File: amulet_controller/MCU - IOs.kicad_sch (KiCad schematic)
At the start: 45 parts, among them U1 STM32G474RET3

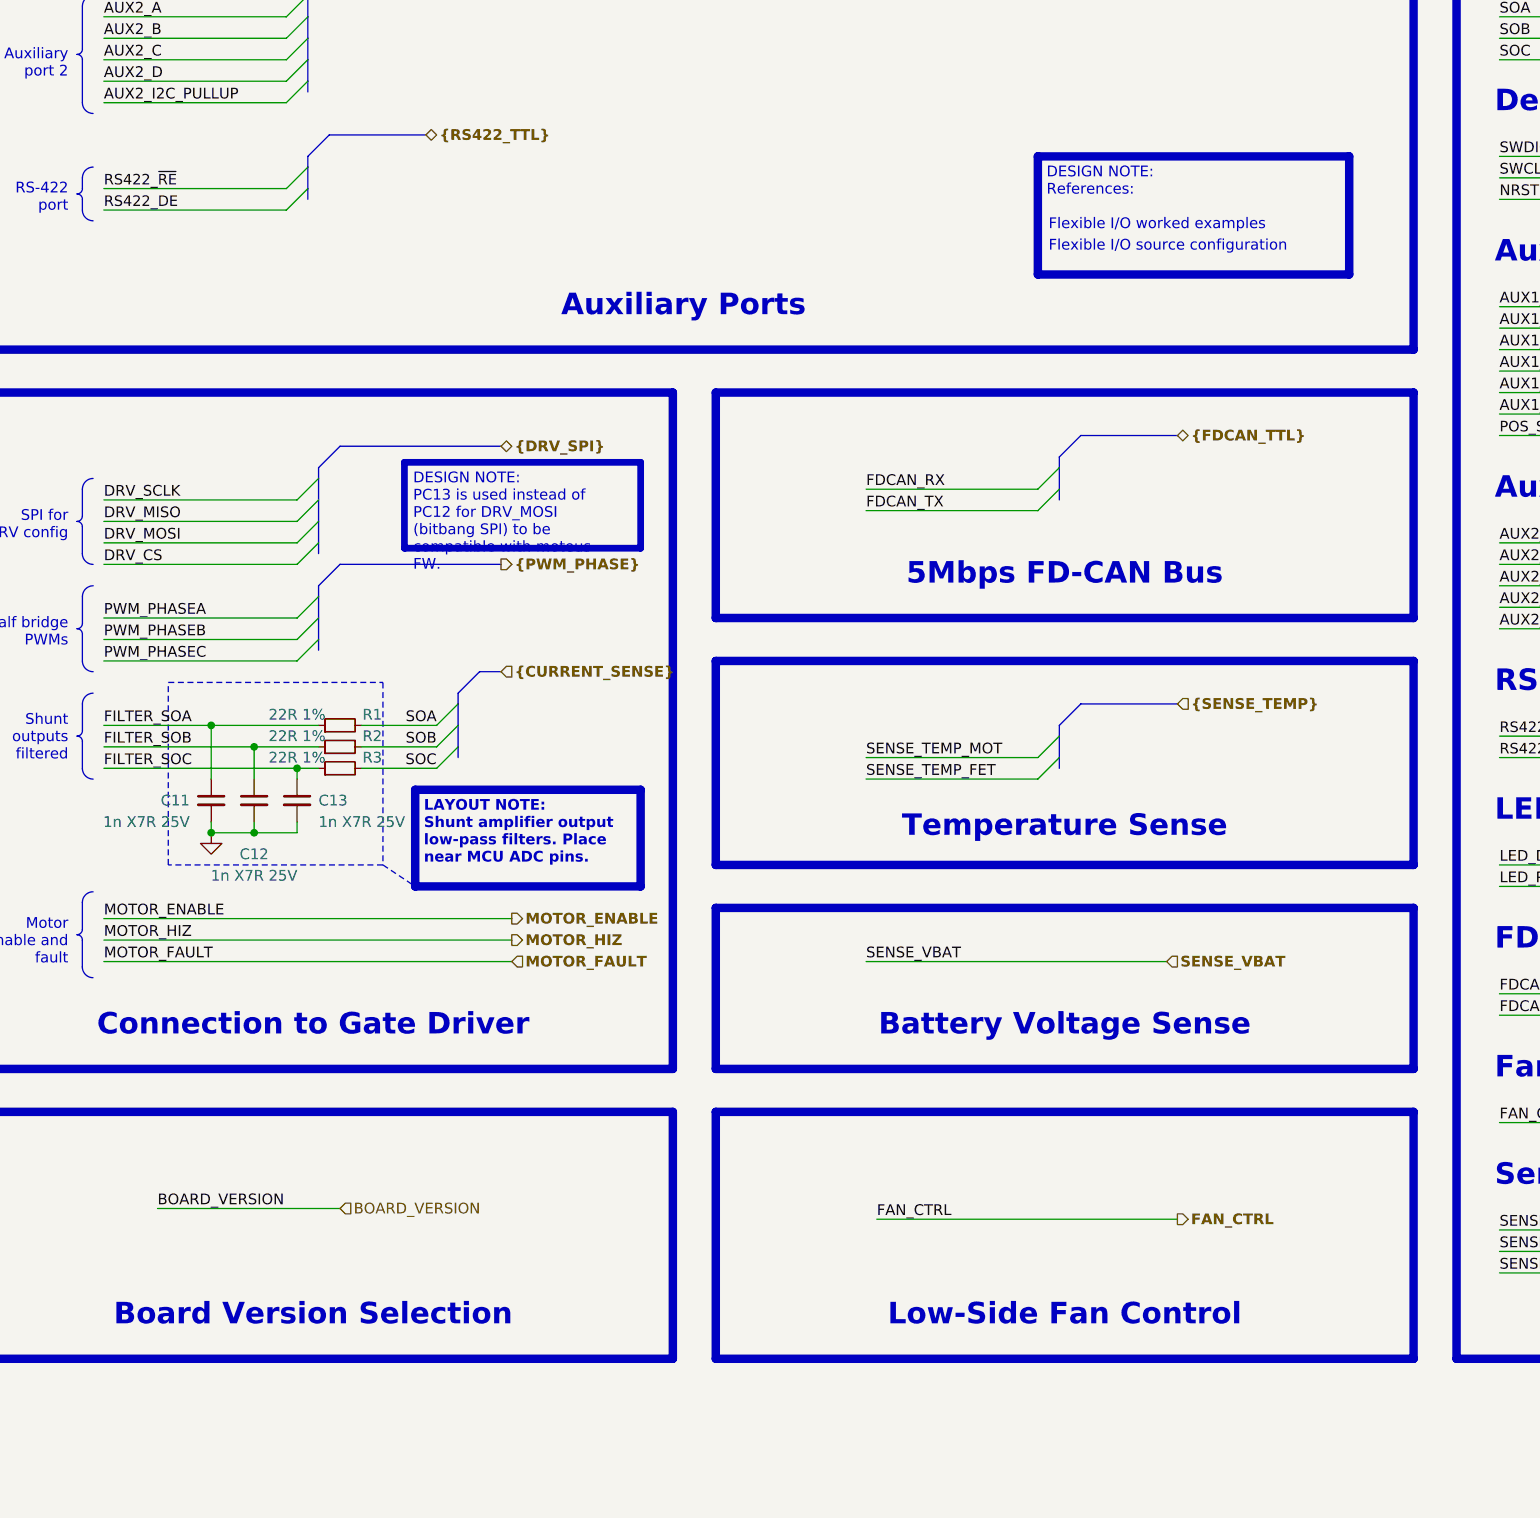
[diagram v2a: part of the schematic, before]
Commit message: finalized pcb. TODO: add clean BOM and KiBot integration
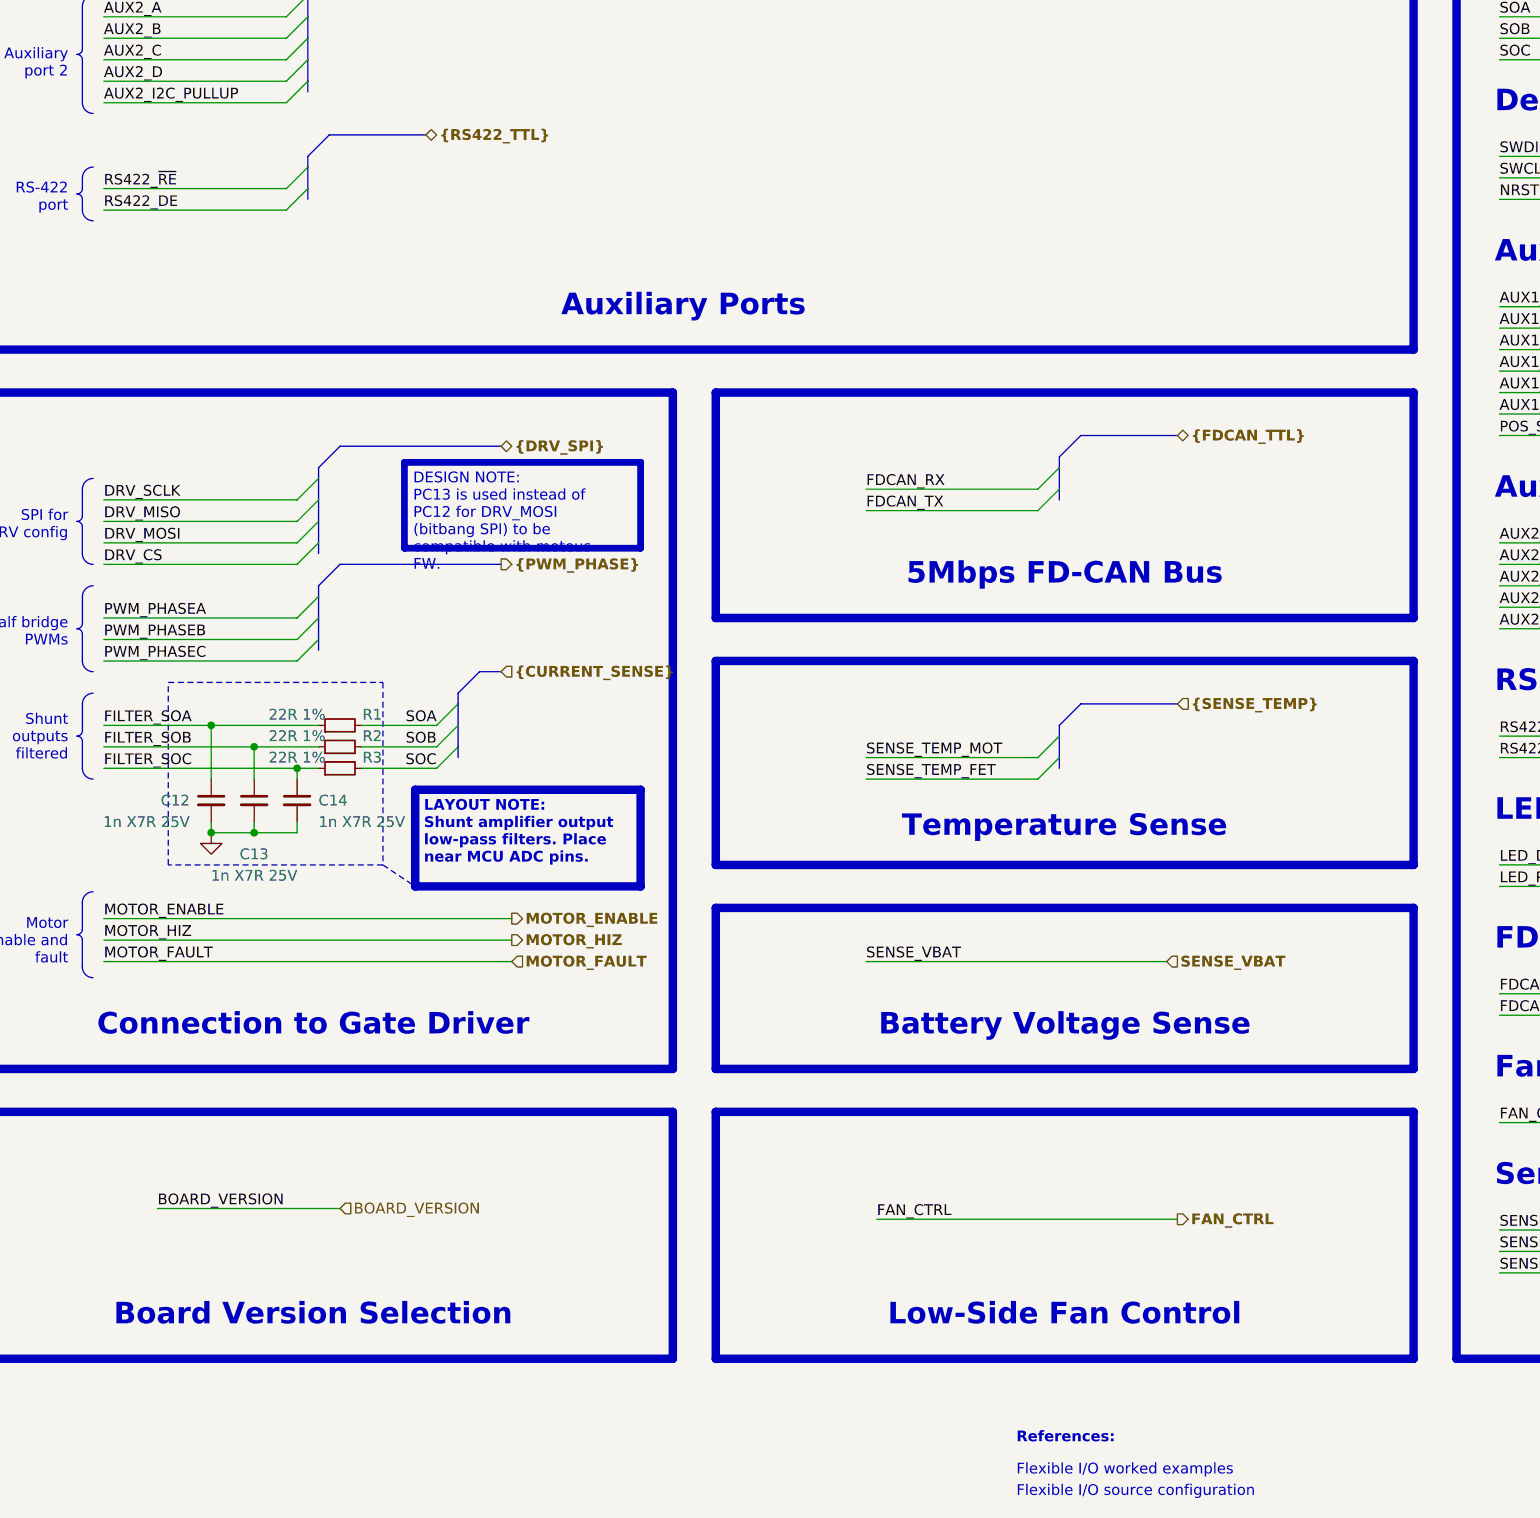
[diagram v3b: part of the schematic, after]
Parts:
- renumbered C11 to C12, C12 to C13, C13 to C14
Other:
- note added: "References:"
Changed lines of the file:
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@@
   (title_block
     (title "MCU - I/Os")
-    (date "2023-10-14")
+    (date "2023-12-20")
     (rev "${REVISION}")
     (company "${COMPANY}")
@@
     (effects (font (size 1.27 1.27) (color 0 0 0 1)) (justify right top))
   )
-  (text_box "DESIGN NOTE:\nReferences:"
-    (at 267.97 97.79 0) (size 36.83 13.97)
-    (stroke (width 1) (type solid) (color 200 200 200 1))
-    (fill (type none))
-    (effects (font (face "Arial") (size 1.27 1.27) (color 0 0 0 1)) (justify left top))
-  )
   (text_box "Auxiliary port 1"
     (at 143.51 60.96 0) (size 10.795 5.715)
@@
     (effects (font (face "Times New Roman") (size 2.54 2.54) (thickness 0.508) bold (color 0 0 0 1)) (justify left bottom))
   )
-  (text "Flexible I/O worked examples" (at 269.24 106.68 0)
+  (text "Flexible I/O worked examples" (at 265.43 254 0)
     (effects (font (face "Arial") (size 1.27 1.27) (color 0 0 0 1)) (justify left bottom) (href "https://jpieper.com/2022/06/30/flexible-i-o-worked-examples/"))
   )
-  (text "Flexible I/O source configuration" (at 269.24 109.22 0)
+  (text "References:" (at 265.43 250.19 0)
+    (effects (font (face "Arial") (size 1.27 1.27) (thickness 0.254) bold (color 0 0 0 1)) (justify left bottom))
+  )
+  (text "Flexible I/O source configuration" (at 265.43 256.54 0)
     (effects (font (face "Arial") (size 1.27 1.27) (color 0 0 0 1)) (justify left bottom) (href "https://jpieper.com/2022/06/28/flexible-i-o-source-configuration/"))
   )
@@
   (symbol (lib_id "Device:C_Small") (at 170.18 173.99 0) (mirror y) (unit 1)
     (in_bom yes) (on_board yes) (dnp no)
-    (property "Reference" "C11" (at 167.64 173.99 0)
+    (property "Reference" "C12" (at 167.64 173.99 0)
       (effects (font (size 1.27 1.27)) (justify left))
     )
@@
       (project "amulet_controller"
         (path "/0650c7a8-acba-429c-9f8e-eec0baf0bc1c/fede4c36-00cc-4d3d-b71c-5243ba232202/e6015f1e-cbce-46f4-85e1-3d5463a17dc1"
-          (reference "C11") (unit 1)
+          (reference "C12") (unit 1)
         )
       )
@@
   (symbol (lib_id "Device:C_Small") (at 175.26 173.99 0) (mirror y) (unit 1)
     (in_bom yes) (on_board yes) (dnp no)
-    (property "Reference" "C12" (at 175.26 180.34 0)
+    (property "Reference" "C13" (at 175.26 180.34 0)
       (effects (font (size 1.27 1.27)))
     )
@@
       (project "amulet_controller"
         (path "/0650c7a8-acba-429c-9f8e-eec0baf0bc1c/fede4c36-00cc-4d3d-b71c-5243ba232202/e6015f1e-cbce-46f4-85e1-3d5463a17dc1"
-          (reference "C12") (unit 1)
+          (reference "C13") (unit 1)
         )
       )
@@
   (symbol (lib_id "Device:C_Small") (at 180.34 173.99 0) (mirror y) (unit 1)
     (in_bom yes) (on_board yes) (dnp no)
-    (property "Reference" "C13" (at 182.88 173.99 0)
+    (property "Reference" "C14" (at 182.88 173.99 0)
       (effects (font (size 1.27 1.27)) (justify right))
     )
@@
       (project "amulet_controller"
         (path "/0650c7a8-acba-429c-9f8e-eec0baf0bc1c/fede4c36-00cc-4d3d-b71c-5243ba232202/e6015f1e-cbce-46f4-85e1-3d5463a17dc1"
-          (reference "C13") (unit 1)
+          (reference "C14") (unit 1)
         )
       )
